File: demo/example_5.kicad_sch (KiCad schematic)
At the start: 6 parts, among them U4 TCA9535PWR, U5 TCA9539PWR

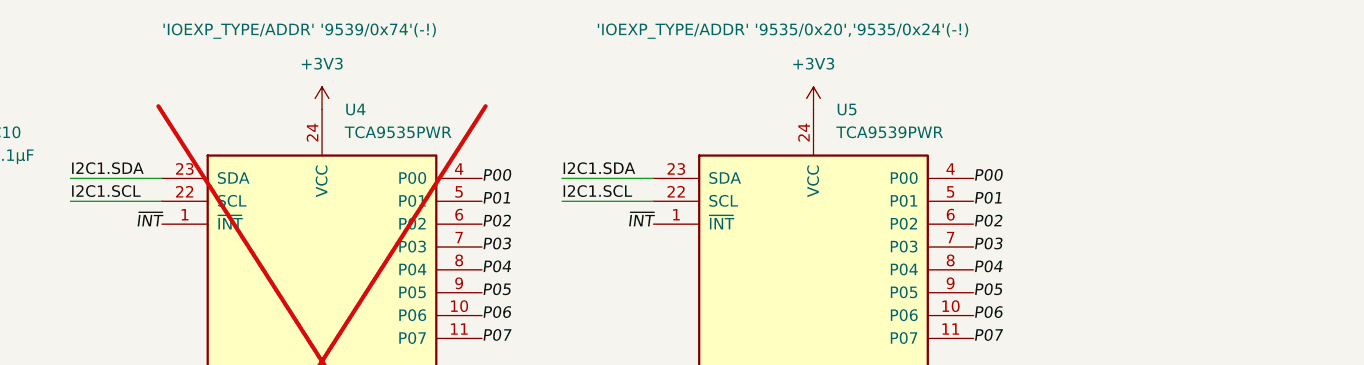
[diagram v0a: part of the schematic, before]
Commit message: Update demo project for upcoming changes
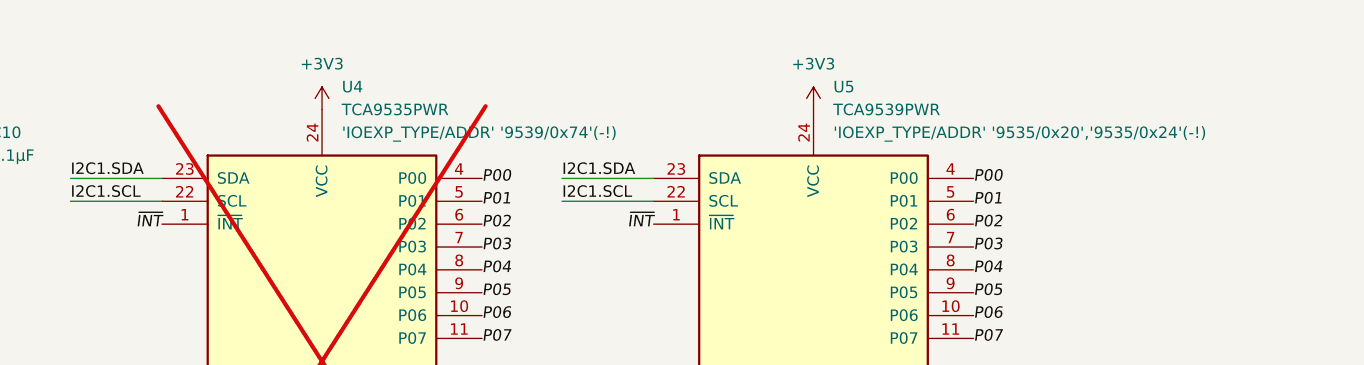
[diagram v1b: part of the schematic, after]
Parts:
- R18: KiVar.Rule 'IOEXP_TYPE/ADDR' '9535/0x24','9539/0x74'(+!) -> (none); Var (none) -> 'IOEXP_TYPE/ADDR' '9535/0x24','9539/0x74'(+!)
- R19: KiVar.Rule 'IOEXP_TYPE/ADDR' '9535/0x20'(+!) -> (none); Var (none) -> 'IOEXP_TYPE/ADDR' '9535/0x20'(+!)
- U4: KiVar.Rule 'IOEXP_TYPE/ADDR' '9539/0x74'(-!) -> (none); Var (none) -> 'IOEXP_TYPE/ADDR' '9539/0x74'(-!)
- U5: KiVar.Rule 'IOEXP_TYPE/ADDR' '9535/0x20','9535/0x24'(-!) -> (none); Var (none) -> 'IOEXP_TYPE/ADDR' '9535/0x20','9535/0x24'(-!)
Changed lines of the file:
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@@
 	(title_block
 		(title "KiVar Demo")
-		(date "2024-03-18")
+		(date "2024-03-19")
 		(rev "0.1.0")
 		(company "Author: Mark Hämmerling <dev@markh.de>")
@@
 			)
 		)
-		(property "KiVar.Rule" "'IOEXP_TYPE/ADDR' '9535/0x24','9539/0x74'(+!)"
+		(property "Var" "'IOEXP_TYPE/ADDR' '9535/0x24','9539/0x74'(+!)"
 			(at 113.03 114.2999 0)
 			(effects
@@
 		(on_board yes)
 		(dnp yes)
+		(fields_autoplaced yes)
 		(property "Reference" "U4"
-			(at 157.48 69.85 0)
+			(at 157.1341 67.31 0)
 			(effects
 				(font
@@
 		)
 		(property "Value" "TCA9535PWR"
-			(at 157.48 72.39 0)
+			(at 157.1341 69.85 0)
 			(effects
 				(font
@@
 			)
 		)
-		(property "KiVar.Rule" "'IOEXP_TYPE/ADDR' '9539/0x74'(-!)"
-			(at 137.16 60.96 0)
+		(property "Var" "'IOEXP_TYPE/ADDR' '9539/0x74'(-!)"
+			(at 157.1341 72.39 0)
 			(effects
 				(font
@@
 		(on_board yes)
 		(dnp no)
+		(fields_autoplaced yes)
 		(property "Reference" "C10"
 			(at 118.11 72.3899 0)
@@
 		(on_board yes)
 		(dnp no)
+		(fields_autoplaced yes)
 		(property "Reference" "U5"
-			(at 212.09 69.85 0)
+			(at 211.7441 67.31 0)
 			(effects
 				(font
@@
 		)
 		(property "Value" "TCA9539PWR"
-			(at 212.09 72.39 0)
+			(at 211.7441 69.85 0)
 			(effects
 				(font
@@
 			)
 		)
-		(property "KiVar.Rule" "'IOEXP_TYPE/ADDR' '9535/0x20','9535/0x24'(-!)"
-			(at 185.42 60.96 0)
+		(property "Var" "'IOEXP_TYPE/ADDR' '9535/0x20','9535/0x24'(-!)"
+			(at 211.7441 72.39 0)
 			(effects
 				(font
@@
 			)
 		)
-		(property "KiVar.Rule" "'IOEXP_TYPE/ADDR' '9535/0x20'(+!)"
+		(property "Var" "'IOEXP_TYPE/ADDR' '9535/0x20'(+!)"
 			(at 113.03 124.4599 0)
 			(effects

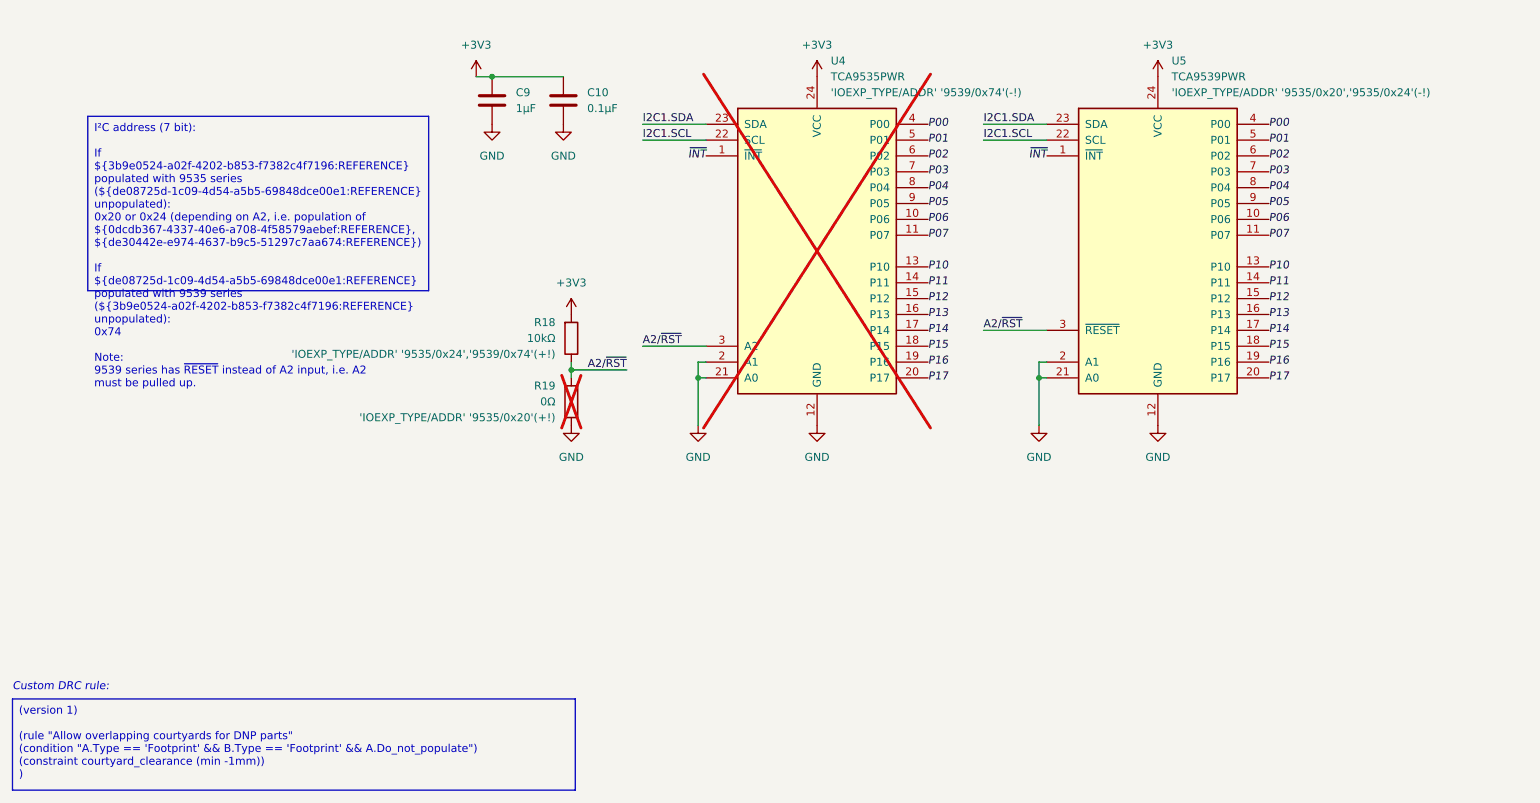
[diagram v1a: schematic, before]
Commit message: Make use of new 0.2.0 features in demo project, use different expression types
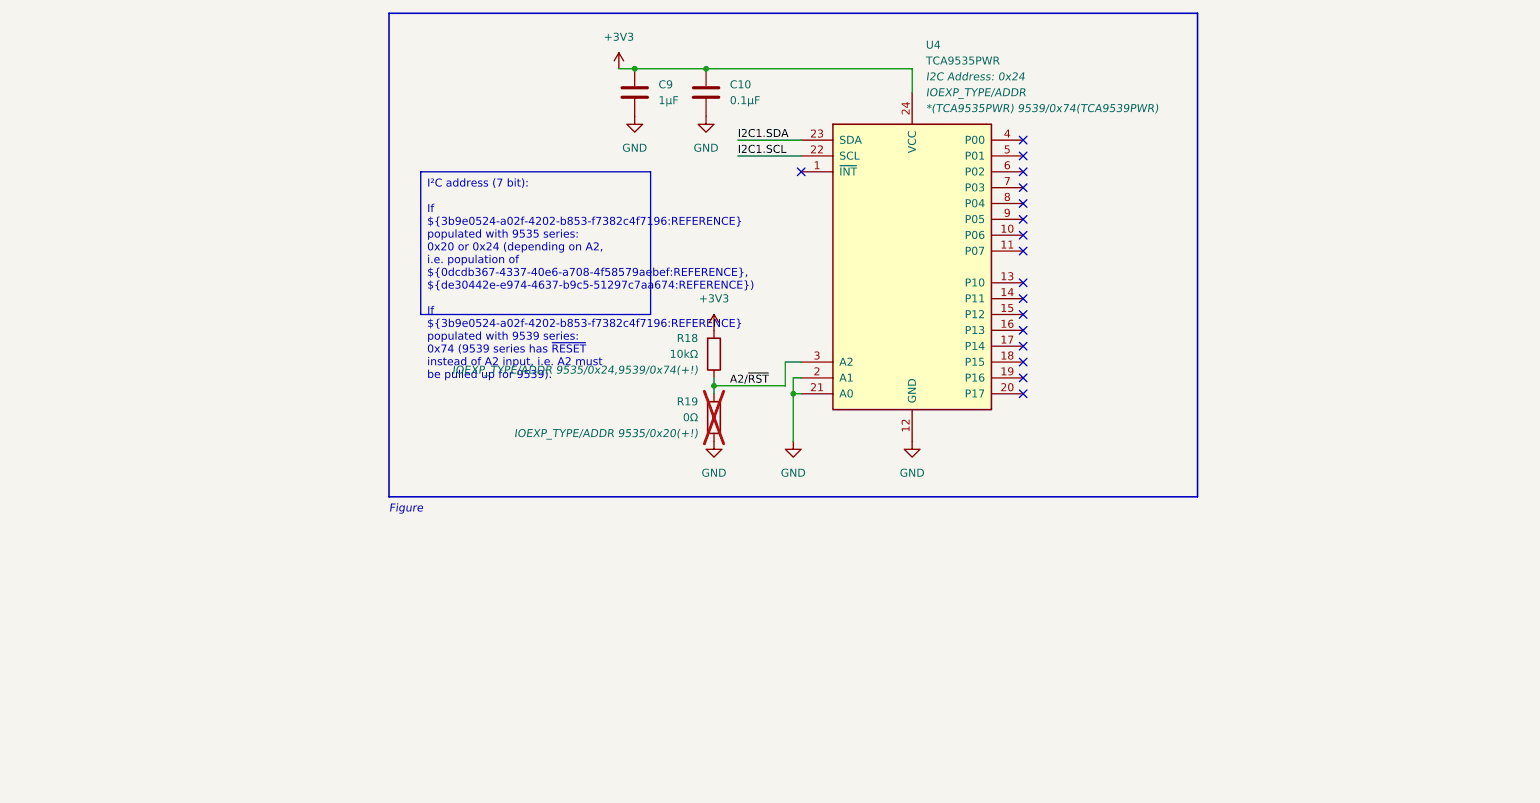
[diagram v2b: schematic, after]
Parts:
- removed U5: TCA9539PWR, Package_SO:TSSOP-24_4.4x7.8mm_P0.65mm, symbol Interface_Expansion:TCA9535PWR
- R18: Var 'IOEXP_TYPE/ADDR' '9535/0x24','9539/0x74'(+!) -> IOEXP_TYPE/ADDR 9535/0x24,9539/0x74(+!)
- R19: Var 'IOEXP_TYPE/ADDR' '9535/0x20'(+!) -> IOEXP_TYPE/ADDR 9535/0x20(+!)
- U4: Datasheet.Var(*) (none) -> http://www.ti.com/lit/ds/symlink/tca9535.pdf; Datasheet.Var(9539/0x74) (none) -> http://www.ti.com/lit/ds/symlink/tca9539.pdf; I2C Address (none) -> 0x24; I2C Address.Var (none) -> 9535/0x20(0x20) 9535/0x24(0x24) 9539/0x74(0x74); MPN (none) -> TCA9535PWR; MPN.Var(*) (none) -> TCA9535PWR; MPN.Var(9539/0x74) (none) -> TCA9539PWR; Manufacturer (none) -> Texas Instruments; Var 'IOEXP_TYPE/ADDR' '9539/0x74'(-!) -> *(TCA9535PWR) 9539/0x74(TCA9539PWR); Var.Aspect (none) -> IOEXP_TYPE/ADDR; now fitted; now in the parts list
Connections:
- net P00: no longer names the net of U4.4 (P00)
- net P01: no longer names the net of U4.5 (P01)
- net P02: no longer names the net of U4.6 (P02)
- net P03: no longer names the net of U4.7 (P03)
- net P04: no longer names the net of U4.8 (P04)
- net P05: no longer names the net of U4.9 (P05)
- net P06: no longer names the net of U4.10 (P06)
- net P07: no longer names the net of U4.11 (P07)
- net P10: no longer names the net of U4.13 (P10)
- net P11: no longer names the net of U4.14 (P11)
- net P12: no longer names the net of U4.15 (P12)
- net P13: no longer names the net of U4.16 (P13)
- net P14: no longer names the net of U4.17 (P14)
- net P15: no longer names the net of U4.18 (P15)
- net P16: no longer names the net of U4.19 (P16)
- net P17: no longer names the net of U4.20 (P17)
- net ~{INT}: no longer names the net of U4.1 (~{INT})
- no-connect marks 0 -> 17
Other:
- note added: "Figure"
- note removed: "Custom DRC rule:"
- moved on the sheet: C10, C9, R18, R19
